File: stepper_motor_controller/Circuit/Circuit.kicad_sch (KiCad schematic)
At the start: 1 part, among them J1 Conn_02x16_Counter_Clockwise

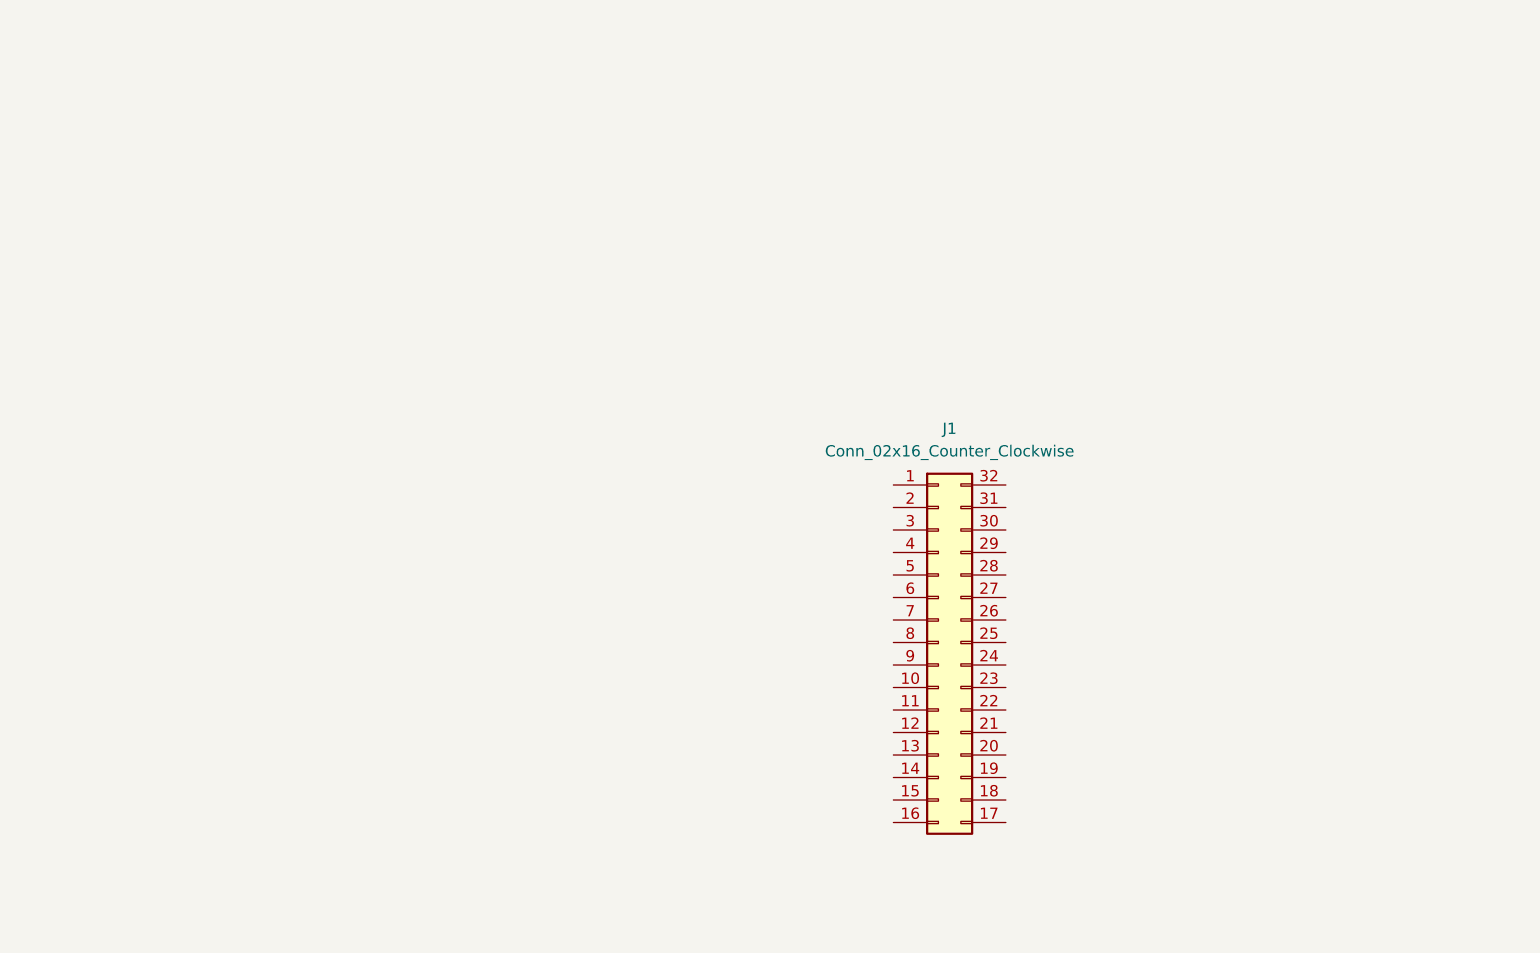
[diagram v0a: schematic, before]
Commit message: added stepper motor controller project
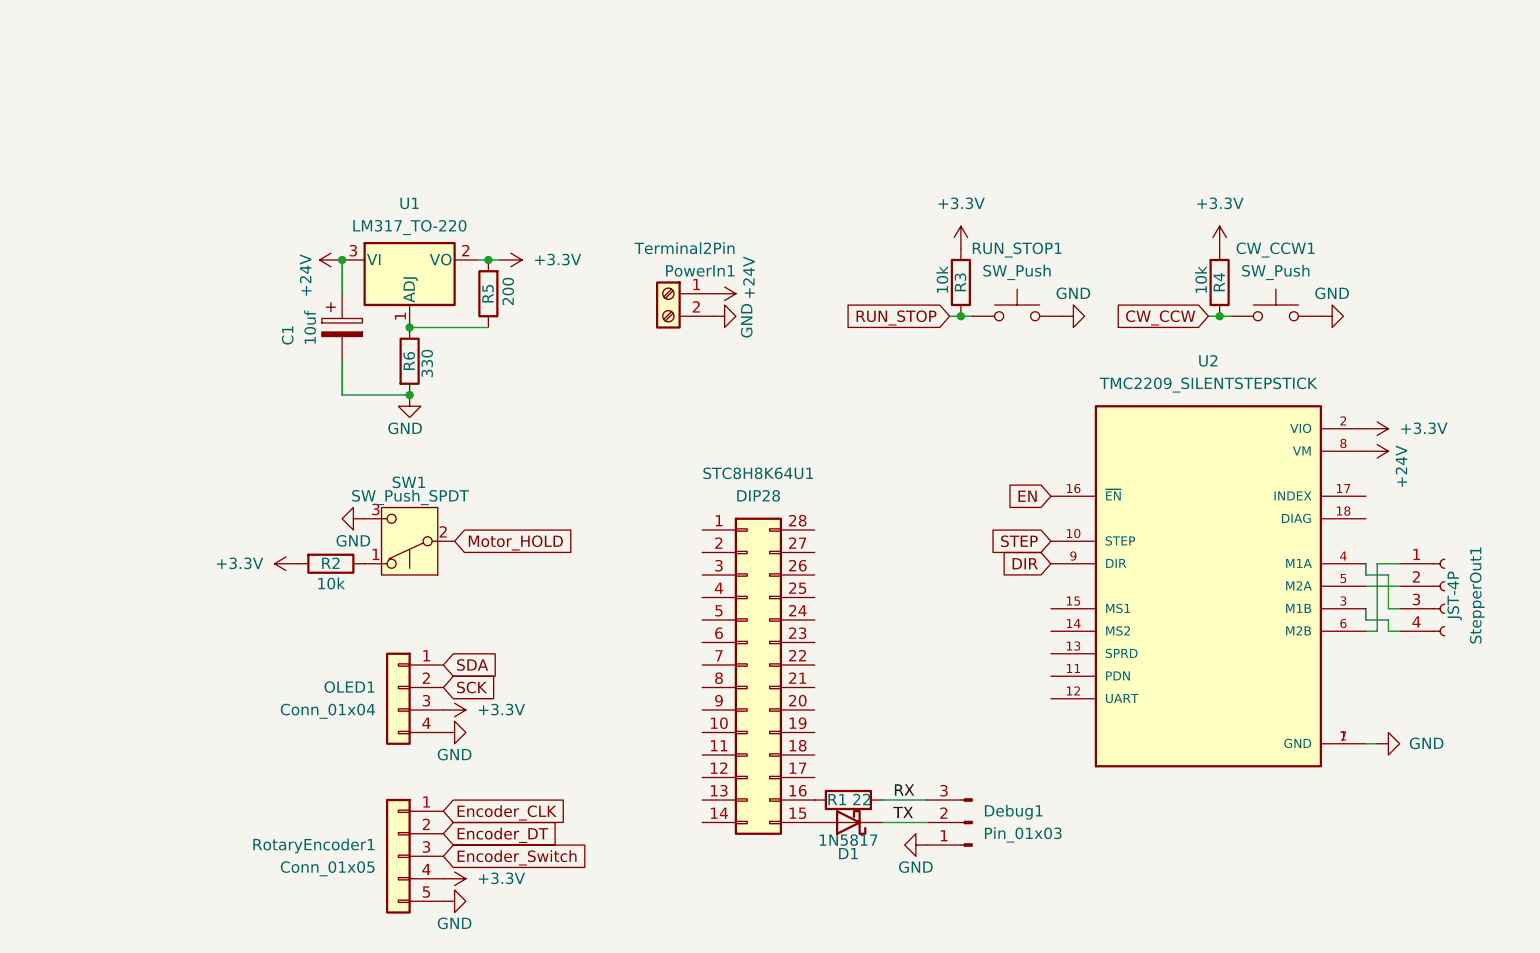
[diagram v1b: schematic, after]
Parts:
- removed J1: Conn_02x16_Counter_Clockwise, symbol Connector_Generic:Conn_02x16_Counter_Clockwise
- added C1: 10uf, symbol Device:C_Polarized
- added CW_CCW1, RUN_STOP1: SW_Push, Resistor_THT:R_Axial_DIN0207_L6.3mm_D2.5mm_P5.08mm_Vertical, symbol Switch:SW_Push
- added D1: 1N5817, Diode_THT:D_DO-41_SOD81_P10.16mm_Horizontal, symbol Diode:1N5817
- added Debug1: Pin_01x03, Connector_PinHeader_2.54mm:PinHeader_1x03_P2.54mm_Vertical, symbol Connector:Conn_01x03_Pin
- added OLED1: Conn_01x04, Connector_PinHeader_2.54mm:PinHeader_1x04_P2.54mm_Vertical, symbol Connector_Generic:Conn_01x04
- added PowerIn1: Terminal2Pin, TerminalBlock:TerminalBlock_bornier-2_P5.08mm, symbol Connector:Screw_Terminal_01x02
- added R1: 22, Resistor_THT:R_Axial_DIN0207_L6.3mm_D2.5mm_P7.62mm_Horizontal, symbol Device:R
- added R2, R3, R4: 10k, Resistor_THT:R_Axial_DIN0207_L6.3mm_D2.5mm_P7.62mm_Horizontal, symbol Device:R
- added R5: 200, Resistor_THT:R_Axial_DIN0207_L6.3mm_D2.5mm_P7.62mm_Horizontal, symbol Device:R
- added R6: 330, Resistor_THT:R_Axial_DIN0207_L6.3mm_D2.5mm_P7.62mm_Horizontal, symbol Device:R
- added RotaryEncoder1: Conn_01x05, Connector_PinHeader_2.54mm:PinHeader_1x05_P2.54mm_Vertical, symbol Connector_Generic:Conn_01x05
- added STC8H8K64U1: DIP28, Package_DIP:DIP-28_W7.62mm_Socket_LongPads, symbol Connector_Generic:Conn_02x14_Counter_Clockwise
- added SW1: SW_Push_SPDT, Connector_PinHeader_2.54mm:PinHeader_1x03_P2.54mm_Vertical, symbol Switch:SW_Push_SPDT
- added StepperOut1: JST-4P, Connector_JST:JST_EH_B4B-EH-A_1x04_P2.50mm_Vertical, symbol Connector:Conn_01x04_Socket
- added U1: LM317_TO-220, Package_TO_SOT_THT:TO-220-3_Vertical, symbol Regulator_Linear:LM317_TO-220
- added U2: TMC2209_SILENTSTEPSTICK, TMC:MODULE_TMC2209_SILENTSTEPSTICK, symbol TMC2209_SILENTSTEPSTICK:TMC2209_SILENTSTEPSTICK
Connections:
- new net: R2.1, SW1.1 (A)
- new net: D1.2 (A), STC8H8K64U1.15 (Pin_15)
- new net: StepperOut1.1 (Pin_1), U2.6 (M2B)
- new net: StepperOut1.2 (Pin_2), U2.5 (M2A)
- new net: StepperOut1.3 (Pin_3), U2.4 (M1A)
- new net: StepperOut1.4 (Pin_4), U2.3 (M1B)
- new net: R1.1, STC8H8K64U1.16 (Pin_16)
- new net: R5.1, R6.1, U1.1 (ADJ)
- new net +24V: C1.1, PowerIn1.1 (Pin_1), U1.3 (VI), U2.8 (VM)
- new net +3.3V: OLED1.3 (Pin_3), R2.2, R3.2, R4.2, R5.2, RotaryEncoder1.4 (Pin_4), U1.2 (VO), U2.2 (VIO)
- new net CW_CCW: CW_CCW1.2, R4.1
- new net DIR: U2.9 (DIR)
- new net EN: U2.16 (~{EN})
- new net Encoder_CLK: RotaryEncoder1.1 (Pin_1)
- new net Encoder_DT: RotaryEncoder1.2 (Pin_2)
- new net Encoder_Switch: RotaryEncoder1.3 (Pin_3)
- new net GND: C1.2, CW_CCW1.1, Debug1.1 (Pin_1), OLED1.4 (Pin_4), PowerIn1.2 (Pin_2), R6.2, RUN_STOP1.1, RotaryEncoder1.5 (Pin_5), SW1.3 (C), U2.1 (GND), U2.7 (GND)
- new net Motor_HOLD: SW1.2 (B)
- new net RUN_STOP: R3.1, RUN_STOP1.2
- new net RX: Debug1.3 (Pin_3), R1.2
- new net SCK: OLED1.2 (Pin_2)
- new net SDA: OLED1.1 (Pin_1)
- new net STEP: U2.10 (STEP)
- new net TX: D1.1 (K), Debug1.2 (Pin_2)

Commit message: stepper motor controller circuit moredevelopment and started the programming
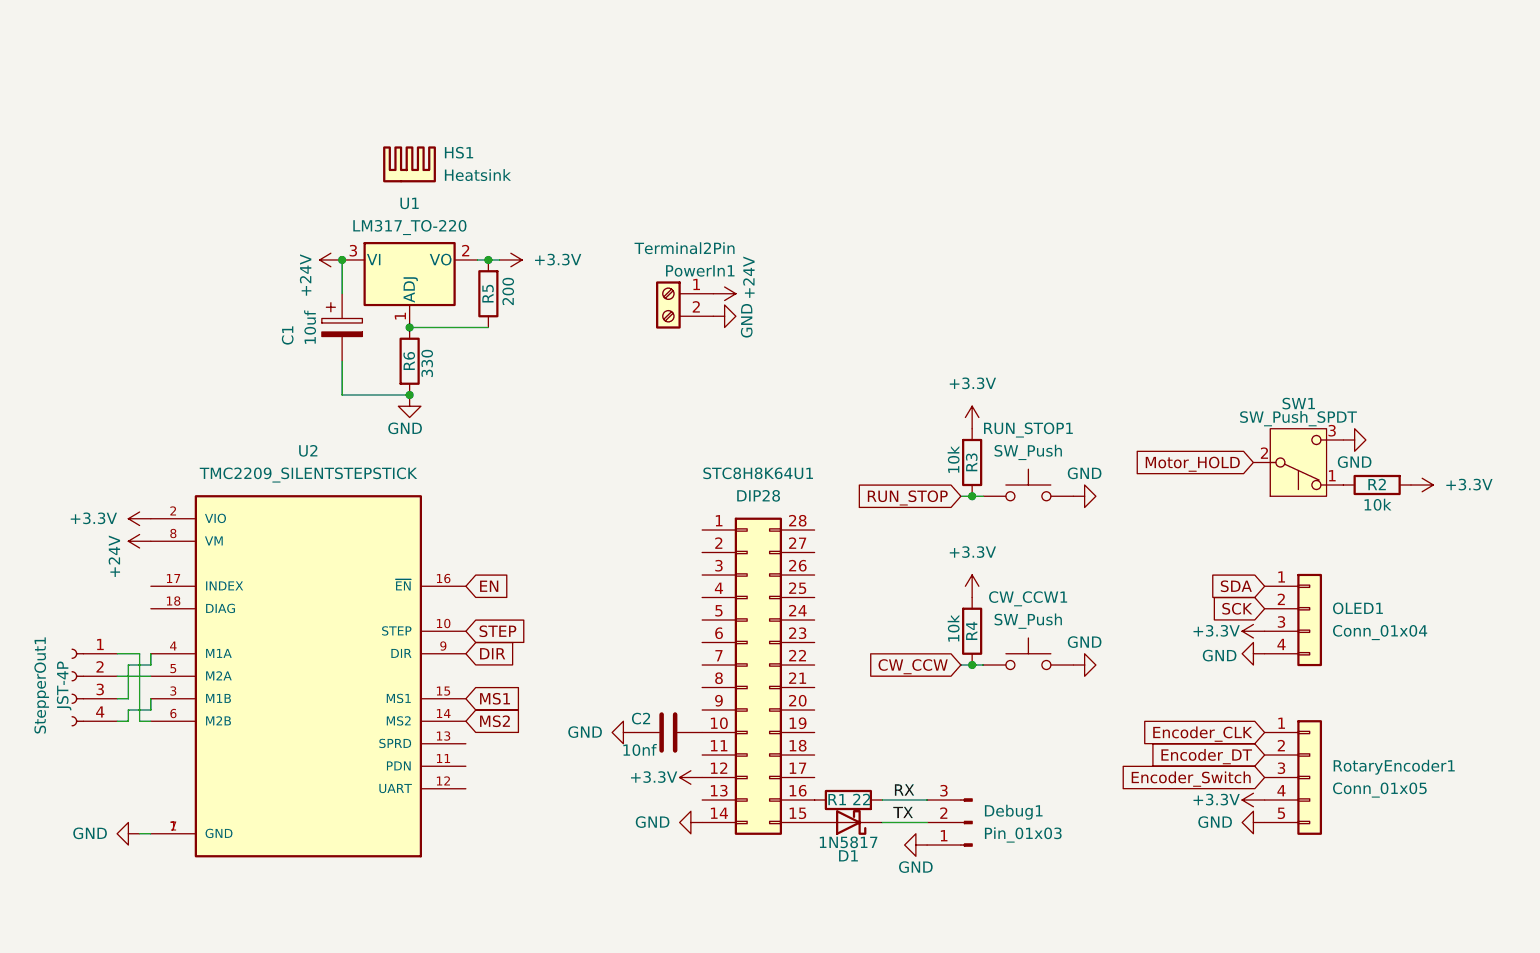
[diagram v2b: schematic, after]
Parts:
- added C2: 10nf, Capacitor_THT:C_Disc_D4.3mm_W1.9mm_P5.00mm, symbol Device:C
- added HS1: Heatsink, symbol Mechanical:Heatsink
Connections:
- net +3.3V: now also STC8H8K64U1.12 (Pin_12)
- net GND: now also STC8H8K64U1.14 (Pin_14), C2.1
- net at STC8H8K64U1.10 (Pin_10): now also C2.2
- net MS2: now reaches U2.14 (MS2)
- net MS1: now reaches U2.15 (MS1)
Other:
- moved on the sheet: CW_CCW1, OLED1, R2, R3, R4, RUN_STOP1, RotaryEncoder1, SW1, StepperOut1, U2

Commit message: finished buttons switches and encoder interfacing for stepper driver
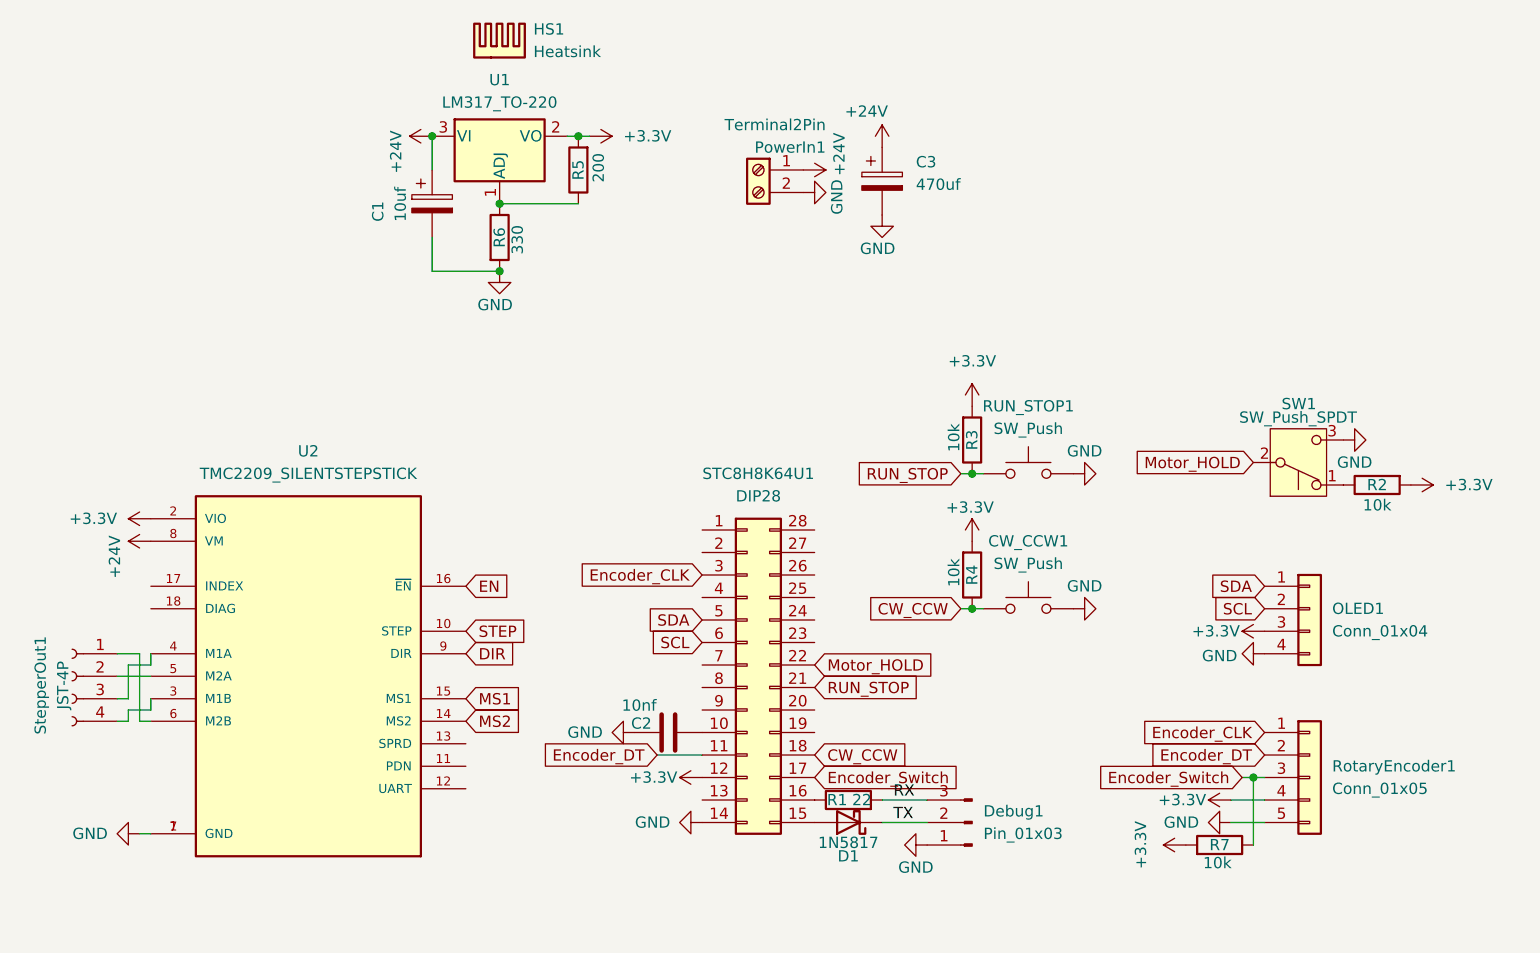
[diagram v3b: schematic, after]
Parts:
- added C3: 470uf, 470uf, symbol Device:C_Polarized
- added R7: 10k, Resistor_THT:R_Axial_DIN0207_L6.3mm_D2.5mm_P7.62mm_Horizontal, symbol Device:R
- D1: footprint Diode_THT:D_DO-41_SOD81_P10.16mm_Horizontal -> Diode_THT:D_DO-41_SOD81_P7.62mm_Horizontal
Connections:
- net SCK is gone; now on net SCL: OLED1.2 (Pin_2)
- net +24V: now also C3.1
- net +3.3V: now also R7.2
- net CW_CCW: now also STC8H8K64U1.18 (Pin_18)
- net Encoder_CLK: now also STC8H8K64U1.3 (Pin_3)
- net Encoder_DT: now also STC8H8K64U1.11 (Pin_11)
- net Encoder_Switch: now also STC8H8K64U1.17 (Pin_17), R7.1
- net GND: now also C3.2
- net Motor_HOLD: now also STC8H8K64U1.22 (Pin_22)
- net RUN_STOP: now also STC8H8K64U1.21 (Pin_21)
- net SDA: now also STC8H8K64U1.5 (Pin_5)
- net SCL: now reaches STC8H8K64U1.6 (Pin_6)
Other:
- moved on the sheet: C1, CW_CCW1, HS1, PowerIn1, R3, R4, R5, R6, RUN_STOP1, U1

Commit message: added stepper motor driver and finished PCB
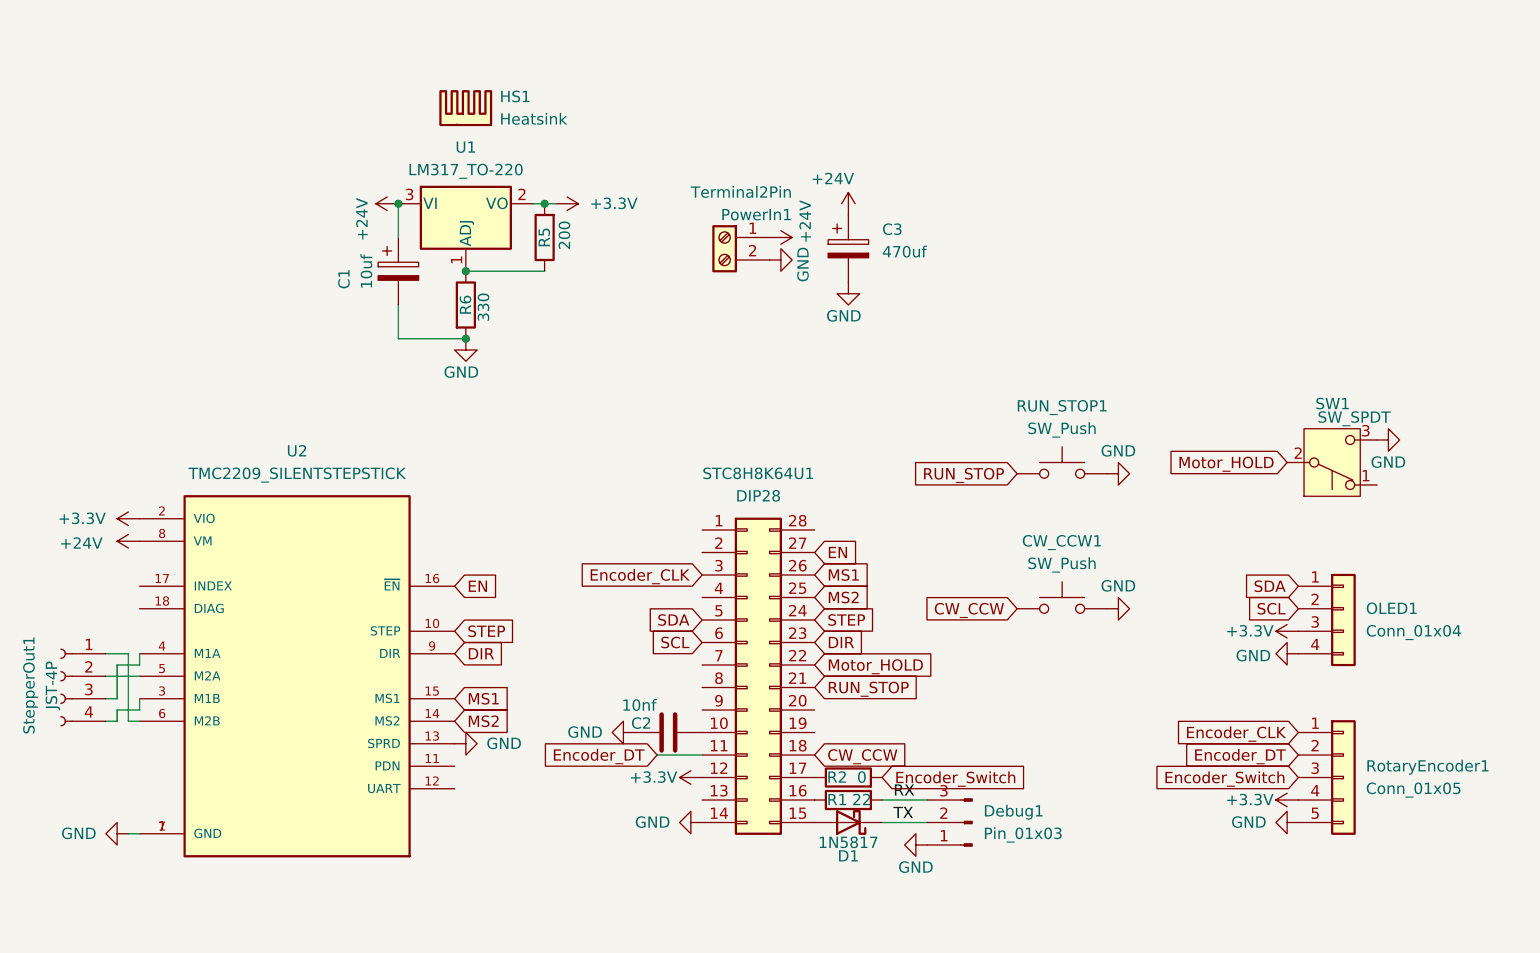
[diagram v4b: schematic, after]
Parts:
- removed R3, R4, R7: 10k, Resistor_THT:R_Axial_DIN0207_L6.3mm_D2.5mm_P7.62mm_Horizontal, symbol Device:R
- C2: footprint Capacitor_THT:C_Disc_D4.3mm_W1.9mm_P5.00mm -> Resistor_THT:R_Axial_DIN0207_L6.3mm_D2.5mm_P7.62mm_Horizontal
- HS1: footprint (none) -> Heatsink:Heatsink_Stonecold_HS-S01_13.21x6.35mm
- R2: value 10k -> 0
- SW1: value SW_Push_SPDT -> SW_SPDT
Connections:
- net +3.3V: no longer R2.2
- net DIR: now also STC8H8K64U1.23 (Pin_23)
- net EN: now also STC8H8K64U1.27 (Pin_27)
- net Encoder_Switch: now also R2.2; no longer STC8H8K64U1.17 (Pin_17)
- net GND: now also U2.13 (SPRD)
- net MS1: now also STC8H8K64U1.26 (Pin_26)
- net MS2: now also STC8H8K64U1.25 (Pin_25)
- net STEP: now also STC8H8K64U1.24 (Pin_24)
- net at SW1.1 (A): no longer R2.1
- new net: R2.1, STC8H8K64U1.17 (Pin_17)
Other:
- moved on the sheet: C1, C3, CW_CCW1, HS1, OLED1, PowerIn1, R5, R6, RUN_STOP1, RotaryEncoder1, SW1, StepperOut1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
